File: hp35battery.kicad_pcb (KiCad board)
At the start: 2 copper layers, 57 x 45 mm, 30 parts, among them J1 USB_B_Micro, J2 PAD+, J3 PAD-, Q1 2N7002, U1 TP4056, U2 MIC5205YM5, U3 MAX40200AUK, U4 DW01A, U5 FS8205

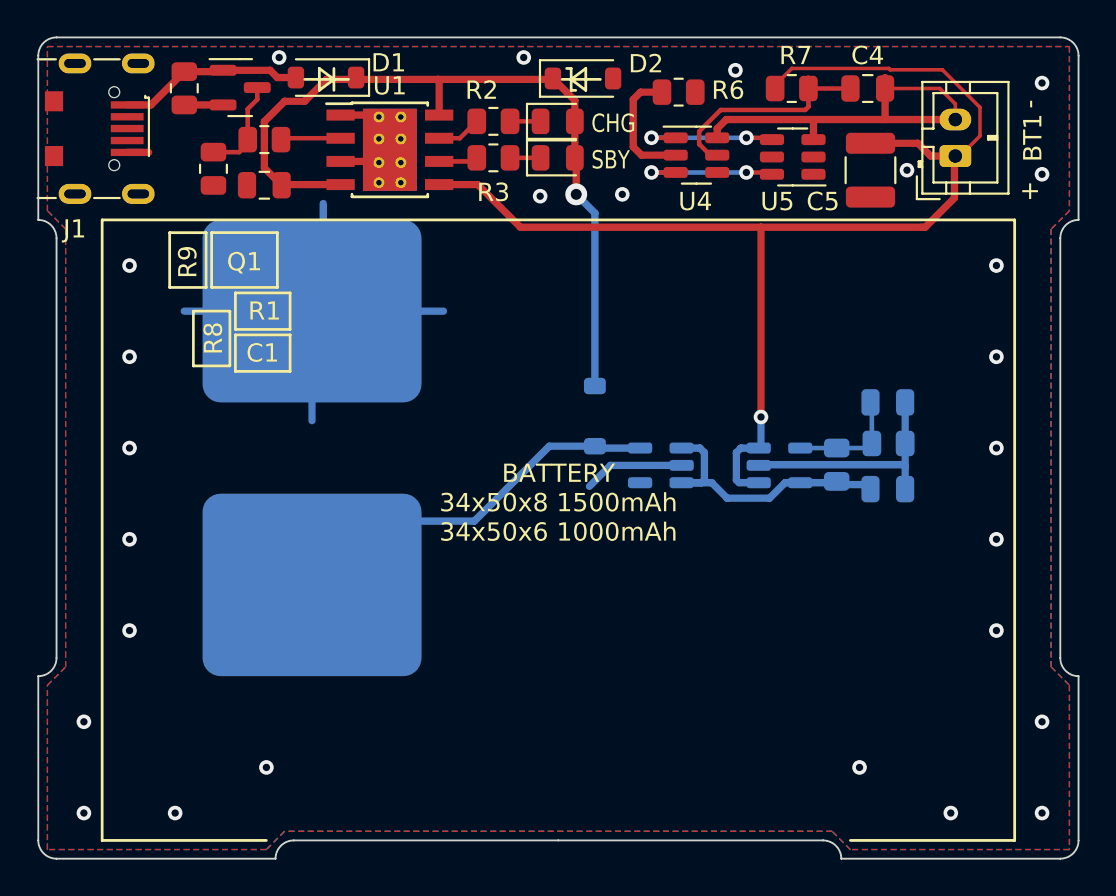
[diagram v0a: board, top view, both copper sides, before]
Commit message: Rev 2.1
Updated to:
* Fit HP67 (reduced length/width, contact size/position)
* Board shape has 1mm recess on all four sides (better case design)
* All components fit on top side
* V2.1: slightly better thermal arrangement for regulator
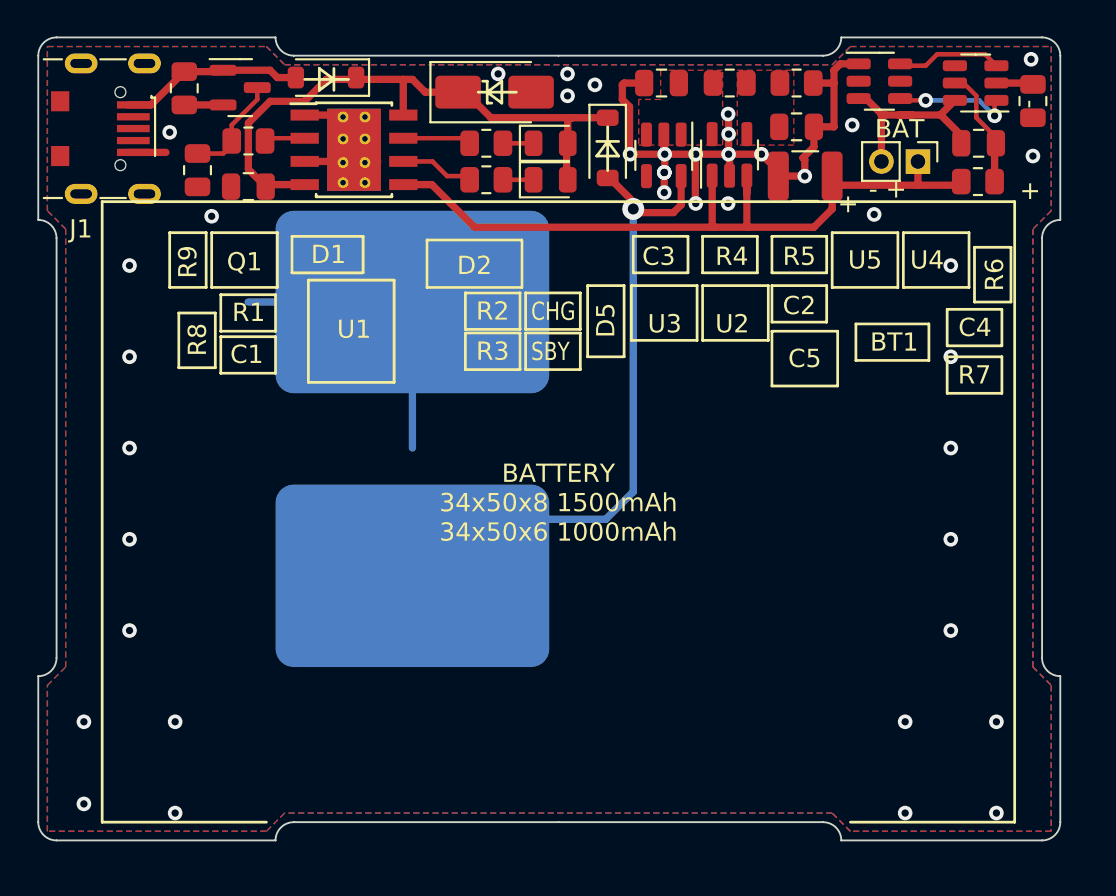
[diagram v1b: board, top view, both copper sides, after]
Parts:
- BT1: value LiPo 3.7V 2000mAh -> LiPo 3.7V 1500mAh; footprint Connector_JST:JST_PH_B2B-PH-K_1x02_P2.00mm_Vertical -> Connector_PinHeader_2.00mm:PinHeader_1x02_P2.00mm_Vertical
- C2, C3, U3: moved to F.Cu
- D1: value 1N5819 -> 1N5817
- D2: value 5V1 -> 5V6; footprint Diode_SMD:D_SOD-123 -> Diode_SMD:D_SMA
- D5: value 1N5819 -> 1N5817; moved to F.Cu
- J2, J3: footprint george:PAD_10x12 -> george:PAD_10x15
- R1: value 5k -> 3k9
- R2, R3: value 1k -> 3k
- R4: value 200k -> 300k; moved to F.Cu
- R5: value 100k -> 150k; moved to F.Cu
- R8: value 20k -> 24k
- R9: value 3k -> 10k
- U2: value MIC5205YM5 -> TPS73101; moved to F.Cu
- U4: value DW01A -> S-8261ABJMD
- moved C3 25.5 mm to (34.1, 2.50), turned to 180 degrees
- moved R4 21.7 mm to (37.9, 2.50), turned to 0 degrees
- moved R5 20.4 mm to (41.5, 2.50)
- moved R6 19.4 mm to (54.5, 3.49), turned to -90 degrees
- moved U2 17.2 mm to (37.9, 6.44), turned to 90 degrees
- moved U3 17.0 mm to (34.3, 6.46), turned to -90 degrees
- moved C2 15.9 mm to (41.5, 4.90)
- moved U4 15.8 mm to (51.4, 2.50), turned to 180 degrees
- moved D5 14.7 mm to (31.2, 6.05)
- moved R7 11.4 mm to (51.5, 7.90)
- moved C4 6.78 mm to (51.5, 5.80), turned to 180 degrees
- moved U5 6.31 mm to (46.1, 2.40), turned to 0 degrees
- moved J2 5.52 mm to (20.5, 29.5)
- moved J3 5.52 mm to (20.5, 14.5)
- moved D2 4.91 mm to (25.0, 3.00)
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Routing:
- net /B+: track 68.5 -> 42.1 mm, vias 1 -> 0
- net /VOUT: track 16.1 -> 31.4 mm, vias 0 -> 1
- net /VREG: track 15.0 -> 0.07 mm
- net /B-: track 22.2 -> 11.0 mm
- net /VCC: track 43.7 -> 32.8 mm, vias 1 -> 0
- net /GND: track 51.7 -> 62.5 mm, vias 26 -> 41
- net /ADJ: track 5.85 -> 0.04 mm
- net /BSENSE: track 12.0 -> 6.19 mm
- net /VM: track 6.85 -> 1.92 mm
- net /G1: track 7.82 -> 5.69 mm, vias 2 -> 0
- net /G2: track 7.82 -> 6.17 mm
- net /STDBY: track 2.14 -> 3.77 mm
- net /PROG: track 3.30 -> 2.03 mm
- net /CHRG: track 2.44 -> 3.36 mm
- added copper zone on F.Cu, net /ADJ
- added copper zone on F.Cu, net /VREG
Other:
- board size 57 x 45 mm -> 56 x 44 mm
- board text added: "- +"
- board text added: "BAT"
- board text added: "HP BATTERY REV2.1 20230928"
- board text removed: "HP BATTERY REV1 20230815"
